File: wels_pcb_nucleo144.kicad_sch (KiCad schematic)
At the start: 29 parts, among them J1 CN8, J10 SERVOMOTOR, J11 I2C PORT, J2 CN7, J3 CN10, J4 CN9, J5 SERVOMOTOR, J6 SD_CARD, J7 MLX90614, J8 MPU6050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

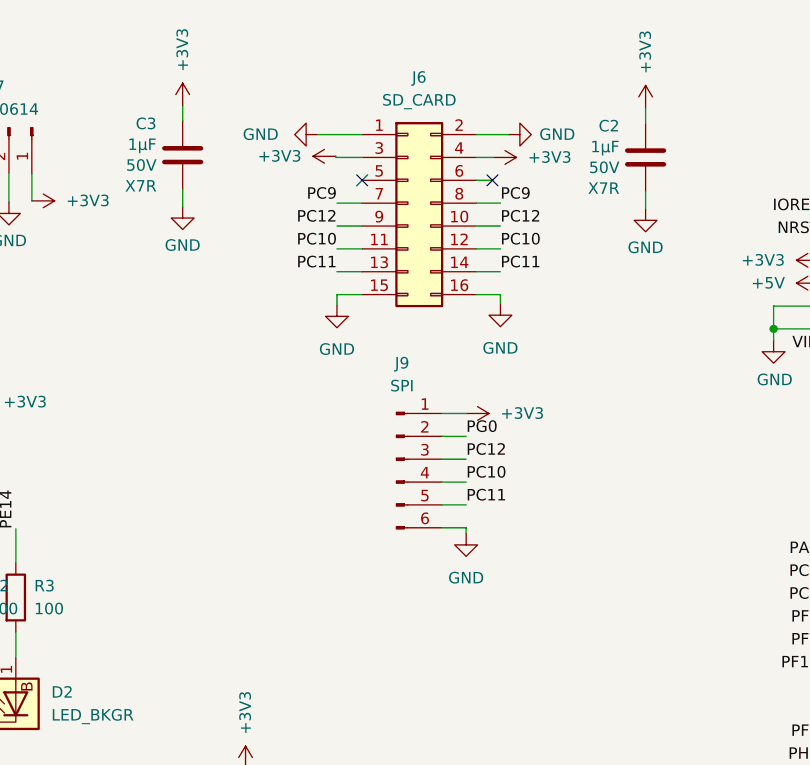
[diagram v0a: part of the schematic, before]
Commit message: Correccion alimentacion 5V para SD Card y cambio de footprint del LED RGB
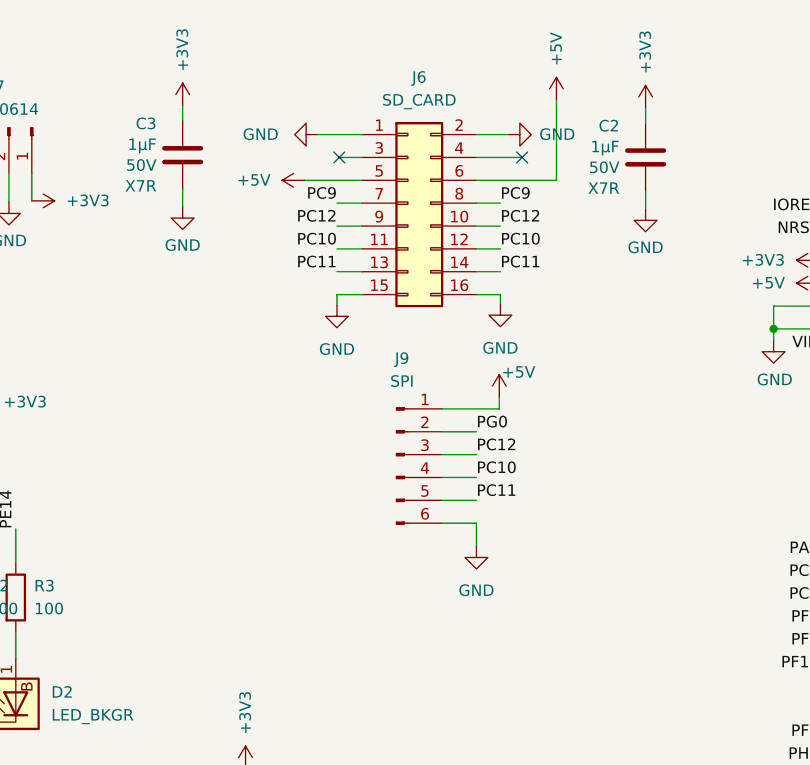
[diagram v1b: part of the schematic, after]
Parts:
- D2: footprint LED_THT:LED_D5.0mm-4_RGB -> LED_THT:LED_D5.0mm-4_RGB_Wide_Pins
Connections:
- net +3V3: no longer J6.3 (Pin_3), J6.4 (Pin_4), J9.1 (Pin_1)
- net +5V: now also J6.5 (Pin_5), J6.6 (Pin_6), J9.1 (Pin_1)
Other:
- moved on the sheet: J9
